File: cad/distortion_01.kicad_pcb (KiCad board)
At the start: 2 copper layers, 89 parts, among them CON101 Ext_PSU, J101 JACK_IN, J102 JACK_OUT, P101 Battery_conn, P102 BYPASS_SWITCH, Q101 BS170, Q102 BS170, Q103 DTC114Y, SW101 OCTAVE_PRE_POST_SWITCH, SW102 HALF-FULLWAVE_SWITCH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

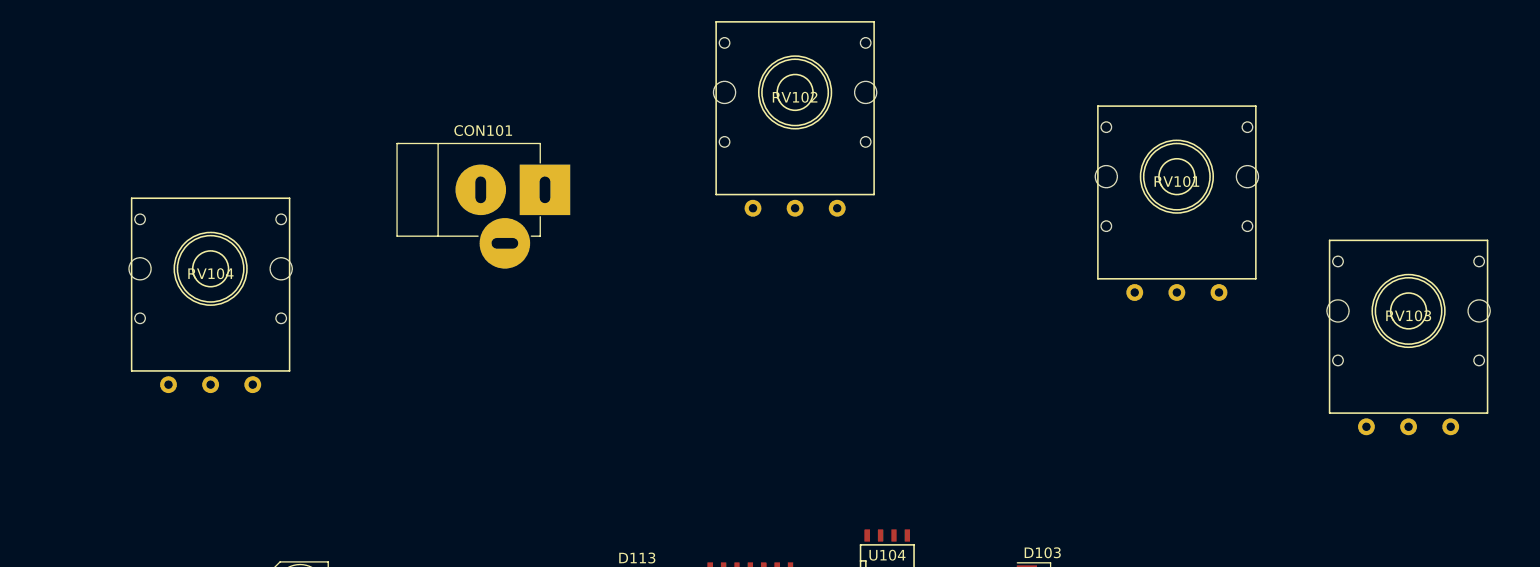
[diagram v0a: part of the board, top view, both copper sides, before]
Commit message: Added names on pots.
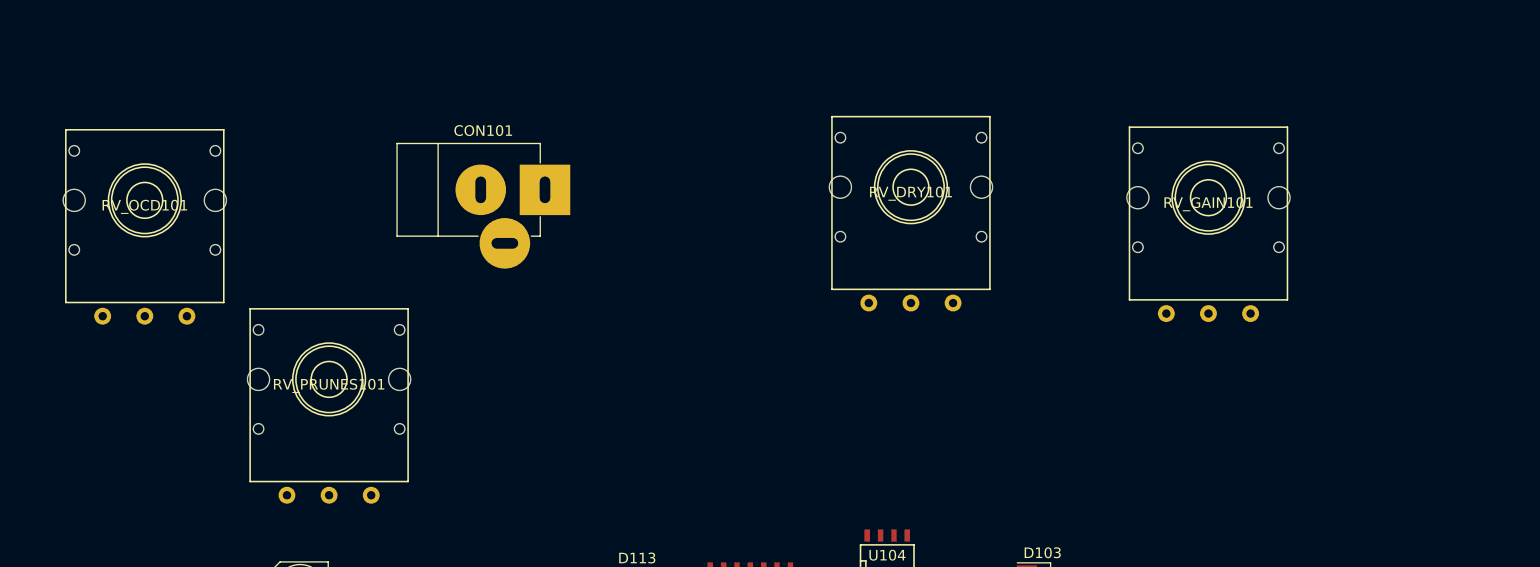
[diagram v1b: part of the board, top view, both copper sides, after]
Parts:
- removed RV101: 1M, flax_lib:alpha_rv141F
- removed RV102, RV103, RV104: 470k, flax_lib:alpha_rv141F
- added RV_DRY101: 470k, flax_lib:alpha_rv141F, F.Cu at (401.8, 40.5)
- added RV_GAIN101: 1M, flax_lib:alpha_rv141F, F.Cu at (430.0, 41.5)
- added RV_OCD101: 470k, flax_lib:alpha_rv141F, F.Cu at (329.0, 41.8)
- added RV_PRUNES101: 470k, flax_lib:alpha_rv141F, F.Cu at (346.5, 58.8)

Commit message: Placement started with 1590B cutout. Too small, 1590BB required.
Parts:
- added C117: 100n, Capacitors_SMD:C_0603_HandSoldering, F.Cu at (67.0, 64.0)
- added C118: 100n, Capacitors_SMD:C_0603_HandSoldering, F.Cu at (79.0, 83.0)
- added C119: 100n, Capacitors_SMD:C_0603_HandSoldering, F.Cu at (67.0, 101.0)
- added C120: 100n, Capacitors_SMD:C_0603_HandSoldering, F.Cu at (85.0, 85.0)
- added C121: 100n, Capacitors_SMD:C_0603_HandSoldering, F.Cu at (67.0, 86.0)
- added C122: 100n, Capacitors_SMD:C_0603_HandSoldering, F.Cu at (49.0, 85.0)
- added C124: 100n, Capacitors_SMD:C_0603_HandSoldering, F.Cu at (67.0, 88.0)
- C102: value 470n -> 100n; footprint Capacitors_SMD:C_0805_HandSoldering -> Capacitors_SMD:C_0603_HandSoldering
- RV_DRY101, RV_GAIN101, RV_OCD101, RV_PRUNES101: footprint flax_lib:alpha_rv141F -> flax_lib:ALPHA_RV09; moved to B.Cu
- moved J101 398.2 mm to (44.0, 111.0), turned to 90 degrees
- moved U103 356.9 mm to (67.0, 60.0), turned to 90 degrees
- moved RV_DRY101 351.2 mm to (51.0, 58.0), turned to 180 degrees
- moved RV_GAIN101 347.4 mm to (83.0, 58.0), turned to 180 degrees
- moved U105 338.6 mm to (67.0, 94.0), turned to 270 degrees
- moved U101 337.9 mm to (79.0, 79.0), turned to 90 degrees
- moved R114 334.3 mm to (51.0, 100.0)
- moved SW102 333.3 mm to (20.0, 116.0)
- moved U102 332.3 mm to (67.0, 107.0), turned to 270 degrees
- moved R106 330.7 mm to (74.0, 61.0)
- moved R107 321.6 mm to (74.0, 58.0), turned to 180 degrees
- moved C110 321.5 mm to (54.0, 105.0)
- moved U107 319.8 mm to (49.0, 89.0), turned to 270 degrees
- moved U106 319.5 mm to (67.0, 79.0), turned to 90 degrees
- moved P101 315.8 mm to (50.0, 119.0)
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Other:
- board outline added: 54 x 81 mm

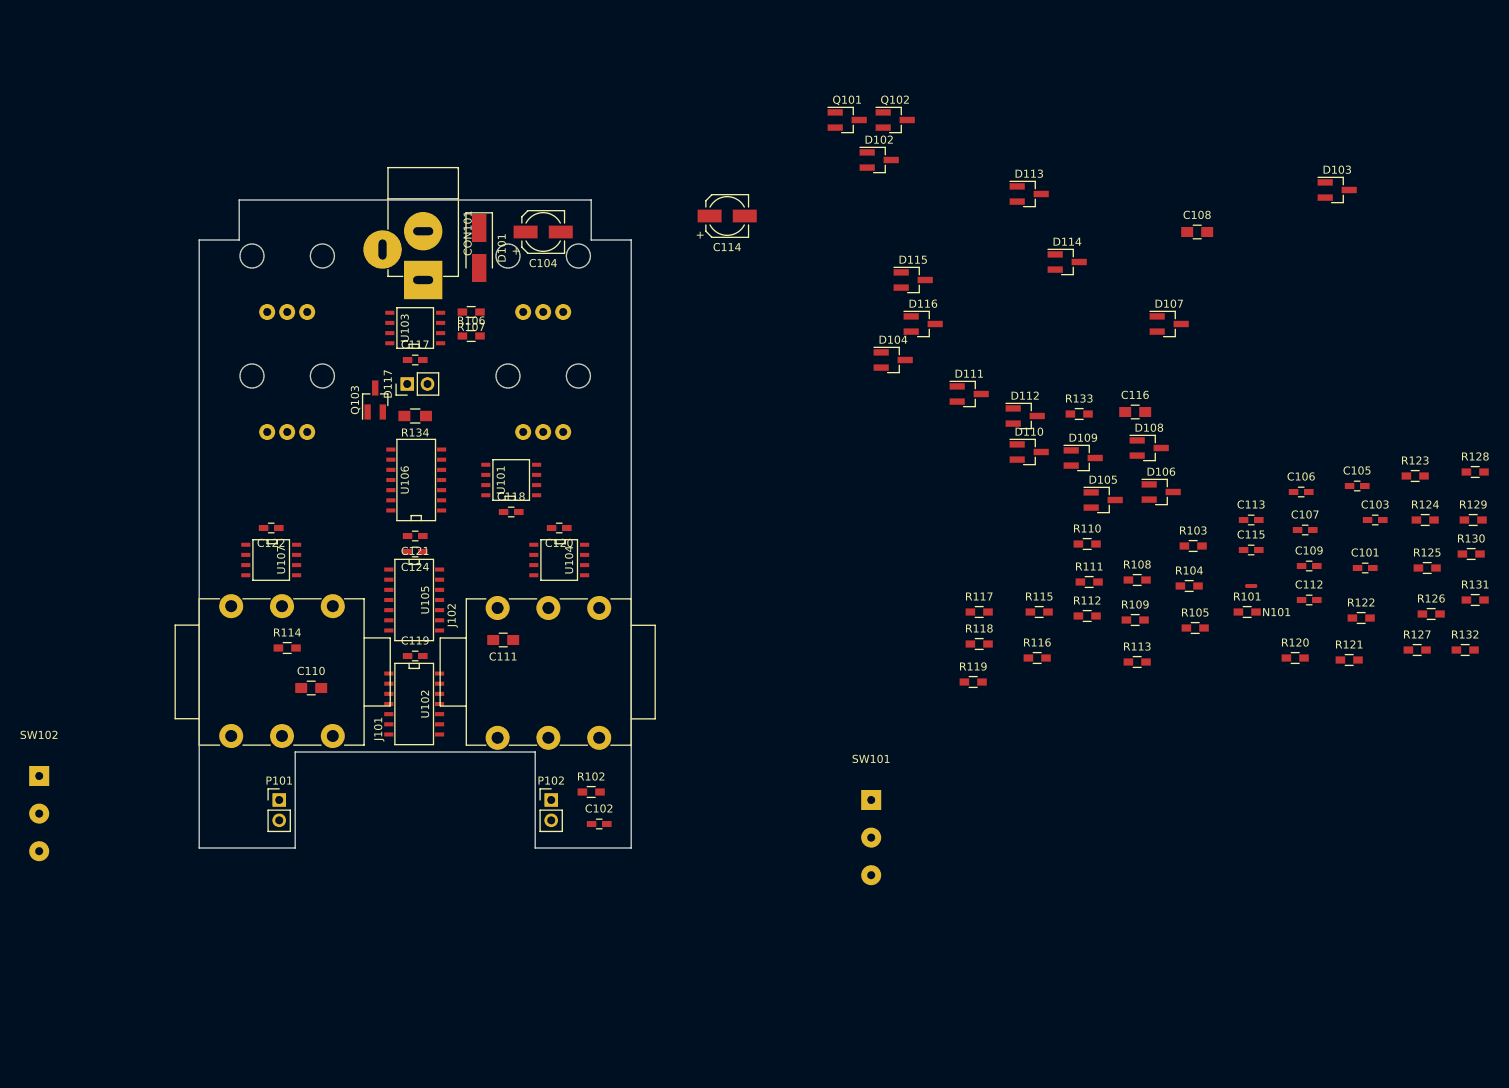
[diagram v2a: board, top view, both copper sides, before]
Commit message: Changed edge cuts to 1590BB. Made pre-placement.
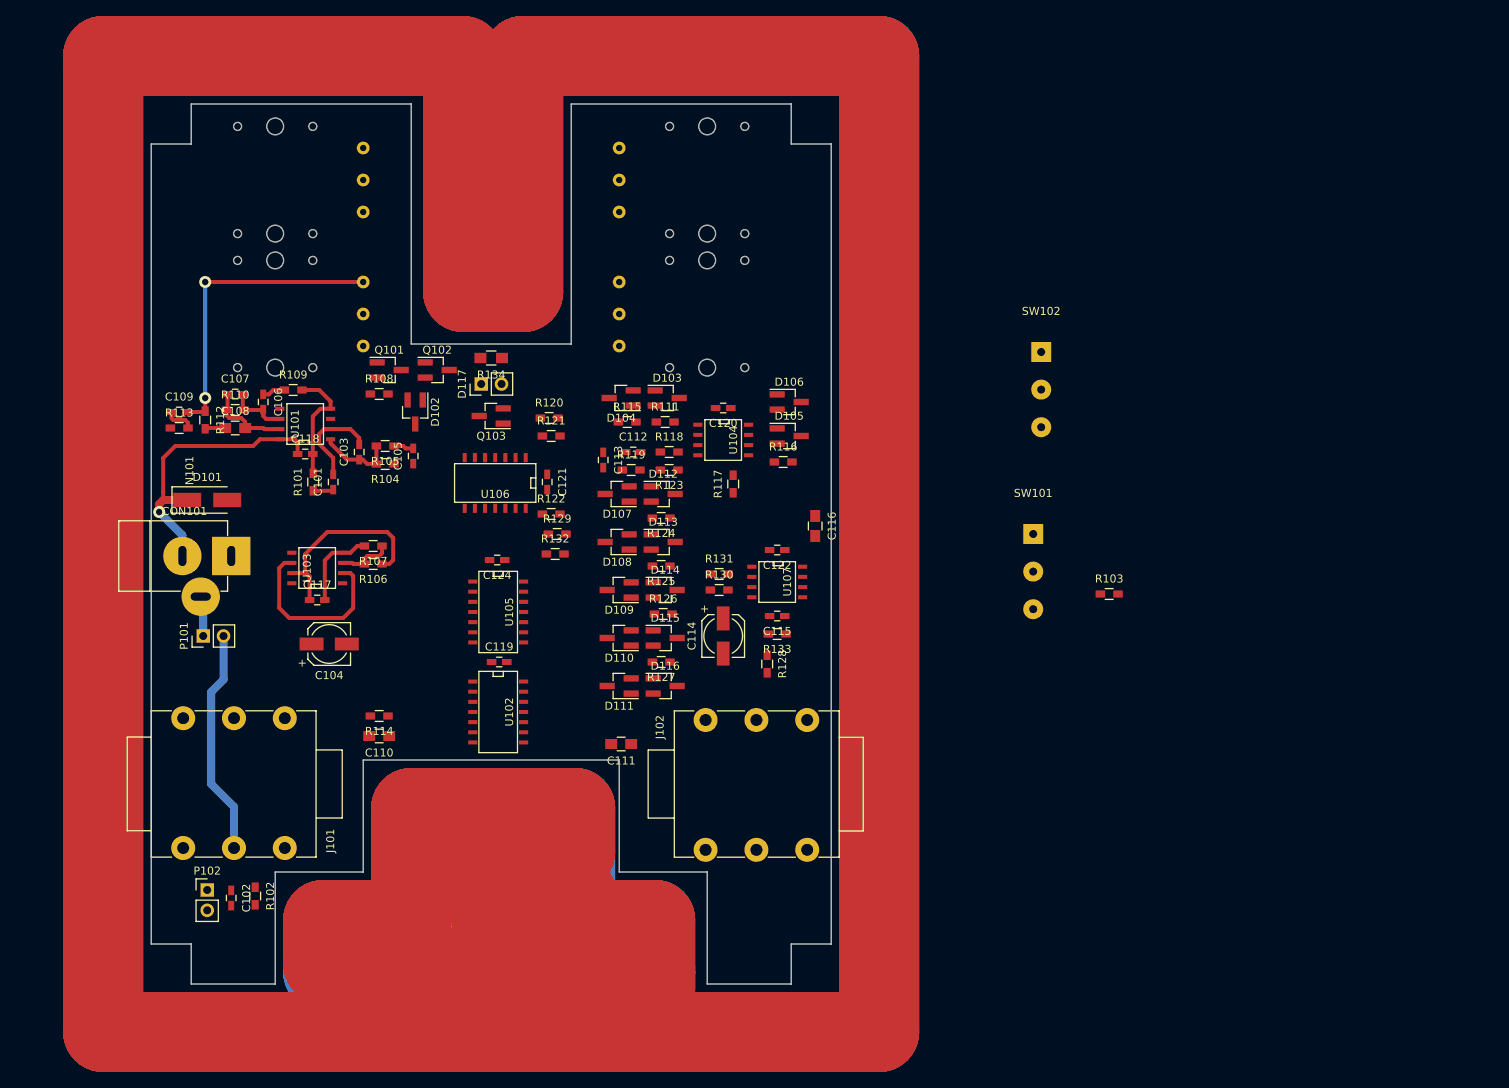
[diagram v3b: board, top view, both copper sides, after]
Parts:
- RV_DRY101, RV_GAIN101, RV_OCD101, RV_PRUNES101: footprint flax_lib:ALPHA_RV09 -> flax_lib:alpha_rv141F
- moved C109 142.6 mm to (37.5, 70.5)
- moved N101 136.5 mm to (35.5, 81.0), turned to 90 degrees
- moved SW102 136.0 mm to (145.2, 63.0)
- moved C107 134.8 mm to (44.5, 68.2)
- moved C106 130.2 mm to (48.0, 69.2), turned to 270 degrees
- moved C101 129.4 mm to (56.8, 79.2), turned to 90 degrees
- moved C103 127.3 mm to (60.0, 75.5), turned to 90 degrees
- moved R113 123.3 mm to (37.5, 72.5)
- moved C108 122.7 mm to (44.5, 72.5)
- moved C105 118.1 mm to (66.8, 76.0), turned to 90 degrees
- moved R101 117.9 mm to (54.2, 79.2), turned to 90 degrees
- moved R129 114.5 mm to (84.8, 85.8)
- moved R132 114.4 mm to (84.5, 88.2)
- moved R112 112.9 mm to (40.8, 71.5), turned to 270 degrees
- moved R109 109.1 mm to (51.8, 67.8)
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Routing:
- net (no net): track 0.00 -> 1312.4 mm
- net +9V: track 0.00 -> 48.2 mm
- net Net-(C109-Pad2): track 0.00 -> 38.2 mm, vias 0 -> 2
- net GNDPWR: track 0.00 -> 28.3 mm
- net GND: track 0.00 -> 25.5 mm
- net VCOM: track 0.00 -> 22.6 mm
- net Net-(C101-Pad2): track 0.00 -> 12.3 mm
- net +BATT: track 0.00 -> 11.4 mm, vias 0 -> 1
- net Net-(C107-Pad1): track 0.00 -> 10.5 mm
- net /audio_gain: track 0.00 -> 9.56 mm
- net Net-(C106-Pad2): track 0.00 -> 7.51 mm
- net Net-(R106-Pad2): track 0.00 -> 6.82 mm
- net Net-(CON101-Pad3): track 0.00 -> 5.05 mm
- net Net-(C109-Pad1): track 0.00 -> 3.73 mm
- net Net-(C106-Pad1): track 0.00 -> 2.88 mm
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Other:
- board size 54 x 81 mm -> 85 x 110 mm
- net class Battery added: clearance 0.2, trace_width 1, via_dia 1.5, via_drill 0.8
- net class Default: trace_width 0.25 -> 0.5; via_dia 0.6 -> 1.5; via_drill 0.4 -> 0.8

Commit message: Finished layout.
Added switch board.
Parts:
- added P103: CONN_01X03, Pin_Headers:Pin_Header_Straight_1x03_Pitch2.54mm, F.Cu at (178.5, 91.0)
- added P104: CONN_01X03, Pin_Headers:Pin_Header_Straight_1x03_Pitch2.54mm, F.Cu at (203.0, 91.0)
- added P105: CONN_01X03, Pin_Headers:Pin_Header_Straight_1x03_Pitch2.54mm, F.Cu at (64.2, 44.2)
- added P106: CONN_01X03, Pin_Headers:Pin_Header_Straight_1x03_Pitch2.54mm, F.Cu at (88.8, 44.2)
- moved R103 94.7 mm to (65.2, 59.5), turned to 90 degrees
- moved SW102 49.3 mm to (190.8, 82.0)
- moved SW101 47.8 mm to (190.8, 97.0)
- moved R102 35.4 mm to (64.0, 100.0), turned to 180 degrees
- moved C102 30.9 mm to (50.5, 101.0)
- moved P102 30.9 mm to (47.5, 100.0)
- moved Q103 4.91 mm to (71.8, 69.8), turned to 90 degrees
- moved R120 4.24 mm to (80.8, 74.2)
- moved C114 3.00 mm to (105.5, 101.5)
- moved R134 2.55 mm to (79.0, 64.2)
- moved C104 1.77 mm to (56.0, 101.2), turned to 90 degrees
- moved R122 1.75 mm to (85.8, 83.2)
- moved R132 1.60 mm to (85.8, 87.2)
- moved R114 1.58 mm to (62.0, 107.0)
- moved R121 1.41 mm to (83.0, 72.5), turned to 180 degrees
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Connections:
- R103 pad 2: Net-(R103-Pad2) -> Net-(P105-Pad2)
- R108 pad 1: Net-(R108-Pad1) -> Net-(P105-Pad3)
- SW101 pad 1: Net-(R108-Pad1) -> Net-(P103-Pad1)
- SW101 pad 2: Net-(R103-Pad2) -> Net-(P103-Pad2)
- SW101 pad 3: Net-(C105-Pad2) -> Net-(P103-Pad3)
- SW102 pad 1: Net-(D106-Pad1) -> Net-(P104-Pad1)
- SW102 pad 2: /audio_octave_out -> Net-(P104-Pad2)
- U101 pad 5: Net-(R108-Pad1) -> Net-(P105-Pad3)
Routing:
- net (no net): track 1312.4 -> 1699.0 mm
- net +9V: track 48.2 -> 266.5 mm, vias 0 -> 10
- net VCOM: track 22.6 -> 240.2 mm, vias 0 -> 14
- net GND: track 25.5 -> 122.9 mm, vias 0 -> 11
- net /audio_gain: track 9.56 -> 100.1 mm
- net /audio_fx_in: track 0.00 -> 77.1 mm, vias 0 -> 2
- net /bypass_cmd: track 0.00 -> 64.3 mm, vias 0 -> 4
- net /audio_octave_out: track 0.00 -> 63.6 mm, vias 0 -> 2
- net Net-(D106-Pad1): track 0.00 -> 53.9 mm, vias 0 -> 3
- net Net-(C105-Pad2): track 2.52 -> 53.8 mm, vias 0 -> 3
- net Net-(C116-Pad1): track 0.00 -> 50.3 mm
- net /audio_prunes_out: track 0.00 -> 48.5 mm, vias 0 -> 2
- net Net-(R104-Pad1): track 0.00 -> 45.3 mm, vias 0 -> 2
- net /audio_ocd_out: track 0.00 -> 43.7 mm, vias 0 -> 2
- net Net-(C115-Pad2): track 0.00 -> 40.5 mm, vias 0 -> 4
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- added copper zone on B.Cu, net GND
- added copper zone on F.Cu, net GND
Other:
- board size 85 x 110 mm -> 179 x 110 mm
- net class Default: trace_width 0.5 -> 10
- board text added: "Randagodron Distortion v1 Main board"
- board text added: "Randagodron Distortion v1 Switch board"

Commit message: Minor corrections.
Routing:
- net GND: track 122.9 -> 140.2 mm
- net /~bypass_cmd~: track 36.4 -> 51.8 mm, vias 2 -> 3
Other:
- net class Default: trace_width 10 -> 0.5
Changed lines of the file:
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@@
   (general
     (links 197)
-    (no_connects 3)
-    (area 33.924999 28.424999 218.575001 142.075001)
+    (no_connects 2)
+    (area 33.924999 31.924999 213.075001 142.075001)
     (thickness 1.6)
     (drawings 71)
-    (tracks 1016)
+    (tracks 1023)
     (zones 0)
     (modules 100)
@@
   )
   (setup
-    (last_trace_width 10)
+    (last_trace_width 0.5)
     (trace_clearance 0.2)
     (zone_clearance 0.25)
@@
   (net_class Default "Ceci est la Netclass par défaut"
     (clearance 0.2)
-    (trace_width 10)
+    (trace_width 0.5)
     (via_dia 1.5)
     (via_drill 0.8)
@@
   (segment (start 86.21 98.04) (end 80.548 98.04) (width 0.5) (layer F.Cu) (net 17))
   (segment (start 86.25 98) (end 86.21 98.04) (width 0.5) (layer F.Cu) (net 17))
+  (segment (start 38 125) (end 38 115) (width 0.5) (layer B.Cu) (net 18) (status 400000))
+  (via (at 38.75 105.75) (size 1.5) (drill 0.8) (layers F.Cu B.Cu) (net 18))
+  (segment (start 40.25 107.25) (end 38.75 105.75) (width 0.5) (layer B.Cu) (net 18))
+  (segment (start 40.25 112.75) (end 40.25 107.25) (width 0.5) (layer B.Cu) (net 18))
+  (segment (start 38 115) (end 40.25 112.75) (width 0.5) (layer B.Cu) (net 18))
   (segment (start 56 99.05) (end 52.3 99.05) (width 0.5) (layer F.Cu) (net 18))
   (via (at 52.25 99) (size 1.5) (drill 0.8) (layers F.Cu B.Cu) (net 18))
@@
   (segment (start 111.3 87.75) (end 109.25 87.75) (width 0.5) (layer F.Cu) (net 18))
   (via (at 109.25 87.75) (size 1.5) (drill 0.8) (layers F.Cu B.Cu) (net 18))
-  (segment (start 38 125) (end 38 128.5) (width 0.5) (layer B.Cu) (net 18))
-  (via (at 38 128.5) (size 1.5) (drill 0.8) (layers F.Cu B.Cu) (net 18))
   (segment (start 116 109) (end 116 107) (width 0.5) (layer B.Cu) (net 18))
   (segment (start 108.45 103.7) (end 105.5 103.7) (width 0.5) (layer F.Cu) (net 18))
@@
   (segment (start 92.5 43.5) (end 94 45) (width 0.5) (layer B.Cu) (net 55))
   (via (at 88.5 70) (size 1.5) (drill 0.8) (layers F.Cu B.Cu) (net 55))
+  (segment (start 74.198 109.27) (end 71.27 109.27) (width 0.5) (layer F.Cu) (net 56) (status 400000))
+  (segment (start 71.25 109.25) (end 71.25 96.75) (width 0.5) (layer B.Cu) (net 56))
+  (via (at 71.25 109.25) (size 1.5) (drill 0.8) (layers F.Cu B.Cu) (net 56))
+  (segment (start 71.27 109.27) (end 71.25 109.25) (width 0.5) (layer F.Cu) (net 56))
   (segment (start 71.25 96.75) (end 70.5 96.75) (width 0.5) (layer B.Cu) (net 56))
   (segment (start 68.75 91) (end 71.25 88.5) (width 0.5) (layer B.Cu) (net 56))
